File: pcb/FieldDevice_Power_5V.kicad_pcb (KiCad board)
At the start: 2 copper layers, 51.6 x 48 mm, 163 parts, among them J1 Itp_1, J2 V in 6-18V, J3 Itp_2, J4 V out 5V, J5 Vtp_2, J6 Vtp_1, J7 Battery, U1 TPS54232

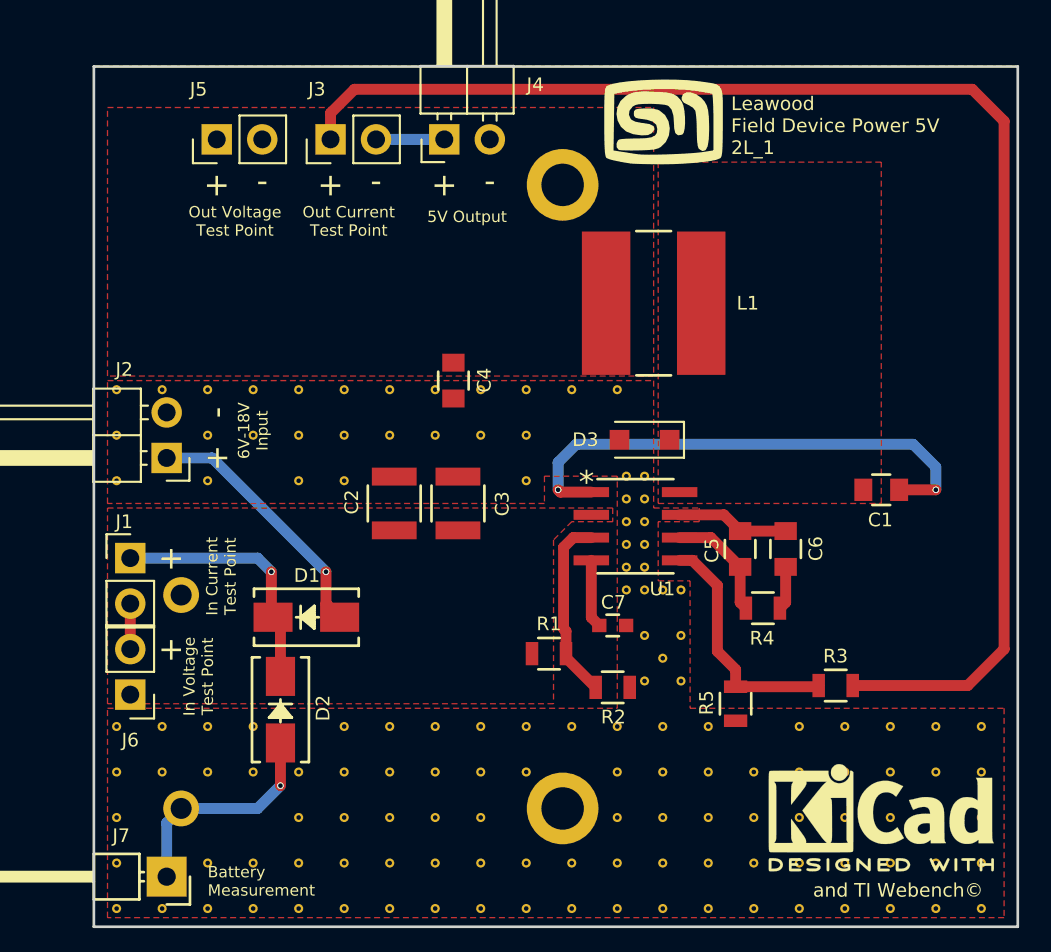
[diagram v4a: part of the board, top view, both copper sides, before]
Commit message: Layout/Assembly corrections for the battery holder
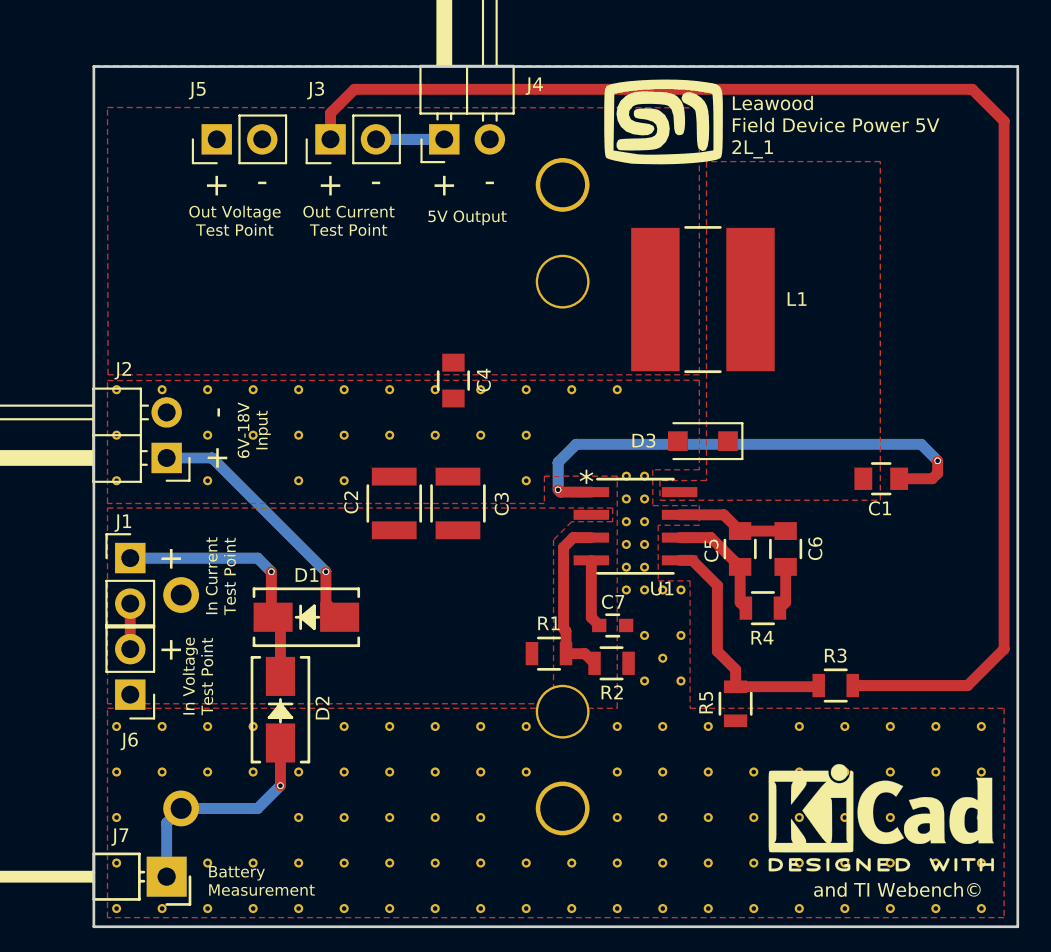
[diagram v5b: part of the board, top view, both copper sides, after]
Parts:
- removed the ST** at (90.7, 81.0)
- moved D3 3.26 mm to (98.0, 65.1)
- moved L1 2.76 mm to (98.0, 57.2)
- moved R2 1.34 mm to (92.9, 77.5)
- moved C1 0.62 mm to (108.0, 67.2)
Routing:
- net /EN: track 10.6 -> 10.1 mm
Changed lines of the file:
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@@
 (kicad_pcb (version 4) (host pcbnew 4.0.7)
   (general
-    (links 177)
+    (links 176)
     (no_connects 0)
     (area 57.142999 37.430999 120.430191 93.8631)
     (thickness 1.6)
     (drawings 24)
-    (tracks 68)
+    (tracks 70)
     (zones 0)
-    (modules 163)
+    (modules 162)
     (nets 15)
   )
@@
   )
   (setup
-    (last_trace_width 0.254)
+    (last_trace_width 0.6096)
     (user_trace_width 0.3048)
     (user_trace_width 0.6096)
@@
     (pad_to_mask_clearance 0)
     (aux_axis_origin 0 0)
-    (visible_elements 7FFEEF7F)
+    (visible_elements 7FFEFF7F)
     (pcbplotparams
       (layerselection 0x010f8_80000001)
@@
   )
   (module FieldDevice_Power_5V:STITCH_VIA (layer F.Cu)
-    (at 90.678 81.026)
-    (fp_text reference ST** (at 0 1.75) (layer F.Fab) hide
-      (effects (font (size 0.762 0.762) (thickness 0.127)))
-    )
-    (fp_text value STITCH_VIA (at 0 -1.5) (layer F.Fab) hide
-      (effects (font (size 0.762 0.762) (thickness 0.127)))
-    )
-    (pad 1 thru_hole circle (at 0 0) (size 0.508 0.508) (drill 0.254) (layers *.Cu)
-      (net 1 GND) (zone_connect 2))
-  )
-  (module FieldDevice_Power_5V:STITCH_VIA (layer F.Cu)
     (at 88.138 81.026)
     (fp_text reference ST** (at 0 1.75) (layer F.Fab) hide
@@
   )
   (module Capacitors_SMD:C_0805 (layer F.Cu)
-    (at 107.95 67.818)
+    (at 107.95 67.2)
     (descr "Capacitor SMD 0805, reflow soldering, AVX (see smccp.pdf)")
     (tags "capacitor 0805")
@@
   )
   (module Resistors_SMD:R_0805 (layer F.Cu)
-    (at 92.964 78.8416)
+    (at 92.9 77.5)
     (descr "Resistor SMD 0805, reflow soldering, Vishay (see dcrcw.pdf)")
     (tags "resistor 0805")
@@
   )
   (module FieldDevice_Power_5V:D_SOD-123F (layer F.Cu)
-    (at 94.742 65.024 180)
+    (at 98 65.1 180)
     (descr D_SOD-123F)
     (tags D_SOD-123F)
@@
     )
   )
-  (module FieldDevice_Power_5V:BC4AAAPC_BATTERYHOLDER_4xAAA locked (layer B.Cu)
-    (at 90.17 50.8 180)
-    (fp_text reference BT1 (at 0 -10 180) (layer B.SilkS)
-      (effects (font (size 0.762 0.762) (thickness 0.127)) (justify mirror))
-    )
-    (fp_text value 6V (at 0 -15 180) (layer B.Fab)
-      (effects (font (size 0.762 0.762) (thickness 0.127)) (justify mirror))
-    )
-    (fp_line (start -25.25 -41.18) (end 25.25 -41.18) (layer B.SilkS) (width 0.15))
-    (fp_line (start 25.25 -41.18) (end 25.25 6.34) (layer B.SilkS) (width 0.15))
-    (fp_line (start 25.25 6.34) (end -25.25 6.34) (layer B.SilkS) (width 0.15))
-    (fp_line (start -25.25 6.34) (end -25.25 -41.18) (layer B.SilkS) (width 0.15))
-    (pad 2 thru_hole circle (at 21.29 -22.89 180) (size 2 2) (drill 1.17) (layers *.Cu *.Mask)
-      (net 1 GND))
-    (pad "" np_thru_hole circle (at 0 -34.8 180) (size 4 4) (drill 2.37) (layers *.Cu *.Mask))
-    (pad "" np_thru_hole circle (at 0 0 180) (size 4 4) (drill 2.37) (layers *.Cu *.Mask))
-    (pad 1 thru_hole circle (at 21.29 -34.8 180) (size 2 2) (drill 1.17) (layers *.Cu *.Mask)
-      (net 2 /BATT))
-  )
   (module FieldDevice_Power_5V:STITCH_VIA (layer F.Cu)
     (at 65.278 62.23)
@@
   )
   (module FieldDevice_Power_5V:SDR0805-6R8ML (layer F.Cu)
-    (at 95.25 57.404 180)
+    (at 98 57.2 180)
     (fp_text reference L1 (at -5.25 0 180) (layer F.SilkS)
       (effects (font (size 0.762 0.762) (thickness 0.127)))
@@
       (xy 1.195199 0.12652) (xy 1.195199 0.12652)) (layer F.SilkS) (width 0.1))
   )
+  (module FieldDevice_Power_5V:BC4AAAPC_BATTERYHOLDER_4xAAA locked (layer B.Cu)
+    (at 90.17 50.8 180)
+    (fp_text reference BT1 (at 0 -10 180) (layer B.SilkS)
+      (effects (font (size 1.5 1.5) (thickness 0.15)) (justify mirror))
+    )
+    (fp_text value 6V (at 0 -15 180) (layer B.Fab)
+      (effects (font (size 1.5 1.5) (thickness 0.15)) (justify mirror))
+    )
+    (fp_text user - (at 18 -22.89 180) (layer B.SilkS)
+      (effects (font (size 2.54 2.54) (thickness 0.254)) (justify mirror))
+    )
+    (fp_circle (center 0 -29.4) (end 3 -29.4) (layer B.CrtYd) (width 0.15))
+    (fp_line (start -25.25 -41.18) (end 25.25 -41.18) (layer B.SilkS) (width 0.15))
+    (fp_line (start 25.25 -41.18) (end 25.25 6.34) (layer B.SilkS) (width 0.15))
+    (fp_line (start 25.25 6.34) (end -25.25 6.34) (layer B.SilkS) (width 0.15))
+    (fp_line (start -25.25 6.34) (end -25.25 -41.18) (layer B.SilkS) (width 0.15))
+    (fp_circle (center 0 -5.4) (end 3 -5.4) (layer B.CrtYd) (width 0.15))
+    (fp_text user + (at 18 -34.8 180) (layer B.SilkS)
+      (effects (font (size 2.54 2.54) (thickness 0.254)) (justify mirror))
+    )
+    (pad 2 thru_hole circle (at 21.29 -22.89 180) (size 2 2) (drill 1.17) (layers *.Cu *.Mask)
+      (net 1 GND))
+    (pad "" np_thru_hole circle (at 0 -34.8 180) (size 3 3) (drill 2.5) (layers *.Cu *.Mask))
+    (pad "" np_thru_hole circle (at 0 0 180) (size 3 3) (drill 2.5) (layers *.Cu *.Mask))
+    (pad 1 thru_hole circle (at 21.29 -34.8 180) (size 2 2) (drill 1.17) (layers *.Cu *.Mask)
+      (net 2 /BATT))
+    (pad "" np_thru_hole circle (at 0 -29.4 180) (size 3 3) (drill 2.74) (layers *.Cu *.Mask))
+    (pad "" np_thru_hole circle (at 0 -5.4 180) (size 3 3) (drill 2.74) (layers *.Cu *.Mask))
+  )
   (gr_text * (at 91.5 67.4) (layer F.SilkS)
     (effects (font (thickness 0.127)))
@@
   (segment (start 68.88 85.6) (end 68.582 85.6) (width 0.6096) (layer F.Cu) (net 2))
   (segment (start 74.422 82.2216) (end 74.422 81.9464) (width 0.6096) (layer F.Cu) (net 2))
-  (segment (start 110.998 67.818) (end 110.998 66.548) (width 0.6096) (layer B.Cu) (net 4))
+  (segment (start 111.1 66.9) (end 110.8 67.2) (width 0.6096) (layer F.Cu) (net 4))
+  (segment (start 110.8 67.2) (end 108.95 67.2) (width 0.6096) (layer F.Cu) (net 4))
+  (segment (start 111.1 66.2) (end 111.1 66.9) (width 0.6096) (layer F.Cu) (net 4))
+  (segment (start 90.932 65.278) (end 110.178 65.278) (width 0.6096) (layer B.Cu) (net 4))
+  (segment (start 110.178 65.278) (end 111.1 66.2) (width 0.6096) (layer B.Cu) (net 4))
+  (via (at 111.1 66.2) (size 0.381) (drill 0.254) (layers F.Cu B.Cu) (net 4))
   (segment (start 89.916 66.294) (end 89.916 67.818) (width 0.6096) (layer B.Cu) (net 4))
-  (segment (start 110.998 66.548) (end 109.728 65.278) (width 0.6096) (layer B.Cu) (net 4))
-  (segment (start 109.728 65.278) (end 90.932 65.278) (width 0.6096) (layer B.Cu) (net 4))
   (segment (start 90.932 65.278) (end 89.916 66.294) (width 0.6096) (layer B.Cu) (net 4))
-  (segment (start 108.95 67.818) (end 110.998 67.818) (width 0.6096) (layer F.Cu) (net 4))
-  (via (at 110.998 67.818) (size 0.381) (drill 0.254) (layers F.Cu B.Cu) (net 4))
   (segment (start 91.7702 67.945) (end 90.043 67.945) (width 0.6096) (layer F.Cu) (net 4))
   (segment (start 90.043 67.945) (end 89.916 67.818) (width 0.6096) (layer F.Cu) (net 4))
@@
   (segment (start 76.962 74.168) (end 77.724 74.93) (width 0.6096) (layer F.Cu) (net 11))
   (via (at 76.962 72.39) (size 0.381) (drill 0.254) (layers F.Cu B.Cu) (net 11))
+  (segment (start 90.358 76.962) (end 91.412 76.962) (width 0.6096) (layer F.Cu) (net 12))
+  (segment (start 91.412 76.962) (end 91.95 77.5) (width 0.6096) (layer F.Cu) (net 12))
   (segment (start 91.7702 70.485) (end 90.764358 70.485) (width 0.6096) (layer F.Cu) (net 12))
   (segment (start 90.764358 70.485) (end 90.220799 71.028559) (width 0.6096) (layer F.Cu) (net 12))
@@
   (segment (start 90.358 75.7024) (end 90.358 76.962) (width 0.6096) (layer F.Cu) (net 12))
   (segment (start 90.358 76.962) (end 90.358 77.1856) (width 0.6096) (layer F.Cu) (net 12))
-  (segment (start 90.358 77.1856) (end 92.014 78.8416) (width 0.6096) (layer F.Cu) (net 12))
   (segment (start 90.358 76.662) (end 90.358 76.962) (width 0.6096) (layer F.Cu) (net 12))
   (segment (start 99.822 78.806) (end 104.394 78.806) (width 0.6096) (layer F.Cu) (net 13))
@@
     (polygon
       (pts
-        (xy 64.77 46.482) (xy 95.25 46.482) (xy 95.25 61.468) (xy 64.77 61.468)
+        (xy 64.77 46.482) (xy 97.8 46.5) (xy 97.8 61.4) (xy 64.8 61.4)
       )
     )
@@
     (polygon
       (pts
-        (xy 95.504 49.53) (xy 95.504 68.58) (xy 107.95 68.58) (xy 107.95 49.53)
+        (xy 98.2 49.5) (xy 98.2 67.3) (xy 95.6 67.3) (xy 95.6 68.4) (xy 107.9 68.4)
+        (xy 107.9 49.5)
       )
     )
@@
     (polygon
       (pts
-        (xy 64.77 61.722) (xy 95.25 61.722) (xy 95.25 68.834) (xy 97.79 68.834) (xy 97.79 69.596)
-        (xy 95.504 69.596) (xy 95.504 72.898) (xy 97.282 72.898) (xy 97.282 80.01) (xy 114.808 80.01)
-        (xy 114.808 91.694) (xy 64.77 91.694) (xy 64.77 80.01) (xy 93.218 80.01) (xy 93.218 67.056)
-        (xy 89.154 67.056) (xy 89.154 68.58) (xy 64.77 68.58)
+        (xy 64.77 61.722) (xy 97.8 61.7) (xy 97.8 66.7) (xy 95.2 66.7) (xy 95.2 68.7)
+        (xy 97.8 68.7) (xy 97.8 69.8) (xy 95.504 69.796) (xy 95.504 72.898) (xy 97.282 72.898)
+        (xy 97.282 80.01) (xy 114.808 80.01) (xy 114.808 91.694) (xy 64.77 91.694) (xy 64.77 80.01)
+        (xy 93.218 80.01) (xy 93.218 67.056) (xy 89.154 67.056) (xy 89.154 68.58) (xy 64.77 68.58)
       )
     )

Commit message: Final changes to layout and off to OSH Park
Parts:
- removed the ST** at (78.0, 81.0)
- removed the ST** at (72.9, 81.0)
- added ST**: STITCH_VIA, FieldDevice_Power_5V:STITCH_VIA, F.Cu at (72.9, 86.1)
- added ST**: STITCH_VIA, FieldDevice_Power_5V:STITCH_VIA, F.Cu at (72.9, 81.0)
- moved D2 2.53 mm to (76.1, 78.2), turned to 0 degrees
- moved D1 0.27 mm to (76.1, 74.8)
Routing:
- net /V+: track 14.2 -> 20.6 mm
- net /BATT: track 13.2 -> 17.9 mm

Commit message: Correct to C4 footprint
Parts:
- removed the ST** at (85.6, 62.2)
- removed the ST** at (83.1, 62.2)
- C4: footprint Capacitors_SMD:C_0805 -> Capacitors_SMD:C_1210
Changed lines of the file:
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@@
     (links 176)
     (no_connects 0)
-    (area 57.142999 37.430999 120.430191 93.8631)
+    (area 63.932999 44.120999 115.645001 92.277001)
     (thickness 1.6)
     (drawings 24)
     (tracks 74)
     (zones 0)
-    (modules 162)
+    (modules 160)
     (nets 15)
   )
@@
   )
   (setup
-    (last_trace_width 0.6096)
+    (last_trace_width 0.254)
     (user_trace_width 0.3048)
     (user_trace_width 0.6096)
@@
     (add_net "Net-(D1-Pad2)")
   )
+  (module Capacitors_SMD:C_1210 (layer F.Cu)
+    (at 84.074 61.722 270)
+    (descr "Capacitor SMD 1210, reflow soldering, AVX (see smccp.pdf)")
+    (tags "capacitor 1210")
+    (attr smd)
+    (fp_text reference C4 (at 0 -2.25 270) (layer F.SilkS)
+      (effects (font (size 1 1) (thickness 0.15)))
+    )
+    (fp_text value "47.0 μF" (at 0 2.5 270) (layer F.Fab)
+      (effects (font (size 1 1) (thickness 0.15)))
+    )
+    (fp_text user %R (at 0 -2.25 270) (layer F.Fab)
+      (effects (font (size 1 1) (thickness 0.15)))
+    )
+    (fp_line (start -1.6 1.25) (end -1.6 -1.25) (layer F.Fab) (width 0.1))
+    (fp_line (start 1.6 1.25) (end -1.6 1.25) (layer F.Fab) (width 0.1))
+    (fp_line (start 1.6 -1.25) (end 1.6 1.25) (layer F.Fab) (width 0.1))
+    (fp_line (start -1.6 -1.25) (end 1.6 -1.25) (layer F.Fab) (width 0.1))
+    (fp_line (start 1 -1.48) (end -1 -1.48) (layer F.SilkS) (width 0.12))
+    (fp_line (start -1 1.48) (end 1 1.48) (layer F.SilkS) (width 0.12))
+    (fp_line (start -2.25 -1.5) (end 2.25 -1.5) (layer F.CrtYd) (width 0.05))
+    (fp_line (start -2.25 -1.5) (end -2.25 1.5) (layer F.CrtYd) (width 0.05))
+    (fp_line (start 2.25 1.5) (end 2.25 -1.5) (layer F.CrtYd) (width 0.05))
+    (fp_line (start 2.25 1.5) (end -2.25 1.5) (layer F.CrtYd) (width 0.05))
+    (pad 1 smd rect (at -1.5 0 270) (size 1 2.5) (layers F.Cu F.Paste F.Mask)
+      (net 6 /Vout))
+    (pad 2 smd rect (at 1.5 0 270) (size 1 2.5) (layers F.Cu F.Paste F.Mask)
+      (net 1 GND))
+    (model Capacitors_SMD.3dshapes/C_1210.wrl
+      (at (xyz 0 0 0))
+      (scale (xyz 1 1 1))
+      (rotate (xyz 0 0 0))
+    )
+  )
   (module FieldDevice_Power_5V:STITCH_VIA (layer F.Cu)
     (at 72.9 86.1)
@@
   (module FieldDevice_Power_5V:STITCH_VIA (layer F.Cu)
     (at 88.138 62.23)
-    (fp_text reference ST** (at 0 1.75) (layer F.Fab) hide
-      (effects (font (size 0.762 0.762) (thickness 0.127)))
-    )
-    (fp_text value STITCH_VIA (at 0 -1.5) (layer F.Fab) hide
-      (effects (font (size 0.762 0.762) (thickness 0.127)))
-    )
-    (pad 1 thru_hole circle (at 0 0) (size 0.508 0.508) (drill 0.254) (layers *.Cu)
-      (net 1 GND) (zone_connect 2))
-  )
-  (module FieldDevice_Power_5V:STITCH_VIA (layer F.Cu)
-    (at 85.598 62.23)
-    (fp_text reference ST** (at 0 1.75) (layer F.Fab) hide
-      (effects (font (size 0.762 0.762) (thickness 0.127)))
-    )
-    (fp_text value STITCH_VIA (at 0 -1.5) (layer F.Fab) hide
-      (effects (font (size 0.762 0.762) (thickness 0.127)))
-    )
-    (pad 1 thru_hole circle (at 0 0) (size 0.508 0.508) (drill 0.254) (layers *.Cu)
-      (net 1 GND) (zone_connect 2))
-  )
-  (module FieldDevice_Power_5V:STITCH_VIA (layer F.Cu)
-    (at 83.058 62.23)
     (fp_text reference ST** (at 0 1.75) (layer F.Fab) hide
       (effects (font (size 0.762 0.762) (thickness 0.127)))
@@
       (at (xyz 0 0 0))
       (scale (xyz 1 1 1))
-      (rotate (xyz 0 0 0))
-    )
-  )
-  (module Capacitors_SMD:C_0805 (layer F.Cu)
-    (at 84.074 61.722 270)
-    (descr "Capacitor SMD 0805, reflow soldering, AVX (see smccp.pdf)")
-    (tags "capacitor 0805")
-    (attr smd)
-    (fp_text reference C4 (at -0.022 -1.726 270) (layer F.SilkS)
-      (effects (font (size 0.762 0.762) (thickness 0.127)))
-    )
-    (fp_text value "47.0 μF" (at 0 2.1 270) (layer F.Fab)
-      (effects (font (size 0.762 0.762) (thickness 0.127)))
-    )
-    (fp_line (start -1 0.625) (end -1 -0.625) (layer F.Fab) (width 0.15))
-    (fp_line (start 1 0.625) (end -1 0.625) (layer F.Fab) (width 0.15))
-    (fp_line (start 1 -0.625) (end 1 0.625) (layer F.Fab) (width 0.15))
-    (fp_line (start -1 -0.625) (end 1 -0.625) (layer F.Fab) (width 0.15))
-    (fp_line (start -1.8 -1) (end 1.8 -1) (layer F.CrtYd) (width 0.05))
-    (fp_line (start -1.8 1) (end 1.8 1) (layer F.CrtYd) (width 0.05))
-    (fp_line (start -1.8 -1) (end -1.8 1) (layer F.CrtYd) (width 0.05))
-    (fp_line (start 1.8 -1) (end 1.8 1) (layer F.CrtYd) (width 0.05))
-    (fp_line (start 0.5 -0.85) (end -0.5 -0.85) (layer F.SilkS) (width 0.15))
-    (fp_line (start -0.5 0.85) (end 0.5 0.85) (layer F.SilkS) (width 0.15))
-    (pad 1 smd rect (at -1 0 270) (size 1 1.25) (layers F.Cu F.Paste F.Mask)
-      (net 6 /Vout))
-    (pad 2 smd rect (at 1 0 270) (size 1 1.25) (layers F.Cu F.Paste F.Mask)
-      (net 1 GND))
-    (model Capacitors_SMD.3dshapes/C_0805.wrl
-      (at (xyz 0 0 0))
-      (scale (xyz 1 1 1))
